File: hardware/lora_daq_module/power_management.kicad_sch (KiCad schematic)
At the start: 36 parts, among them J7 Conn_01x02, U6 MCP1700x-330xxTT, U7 TPS2116DRL, U8 TPS63002, U9 MCP73833

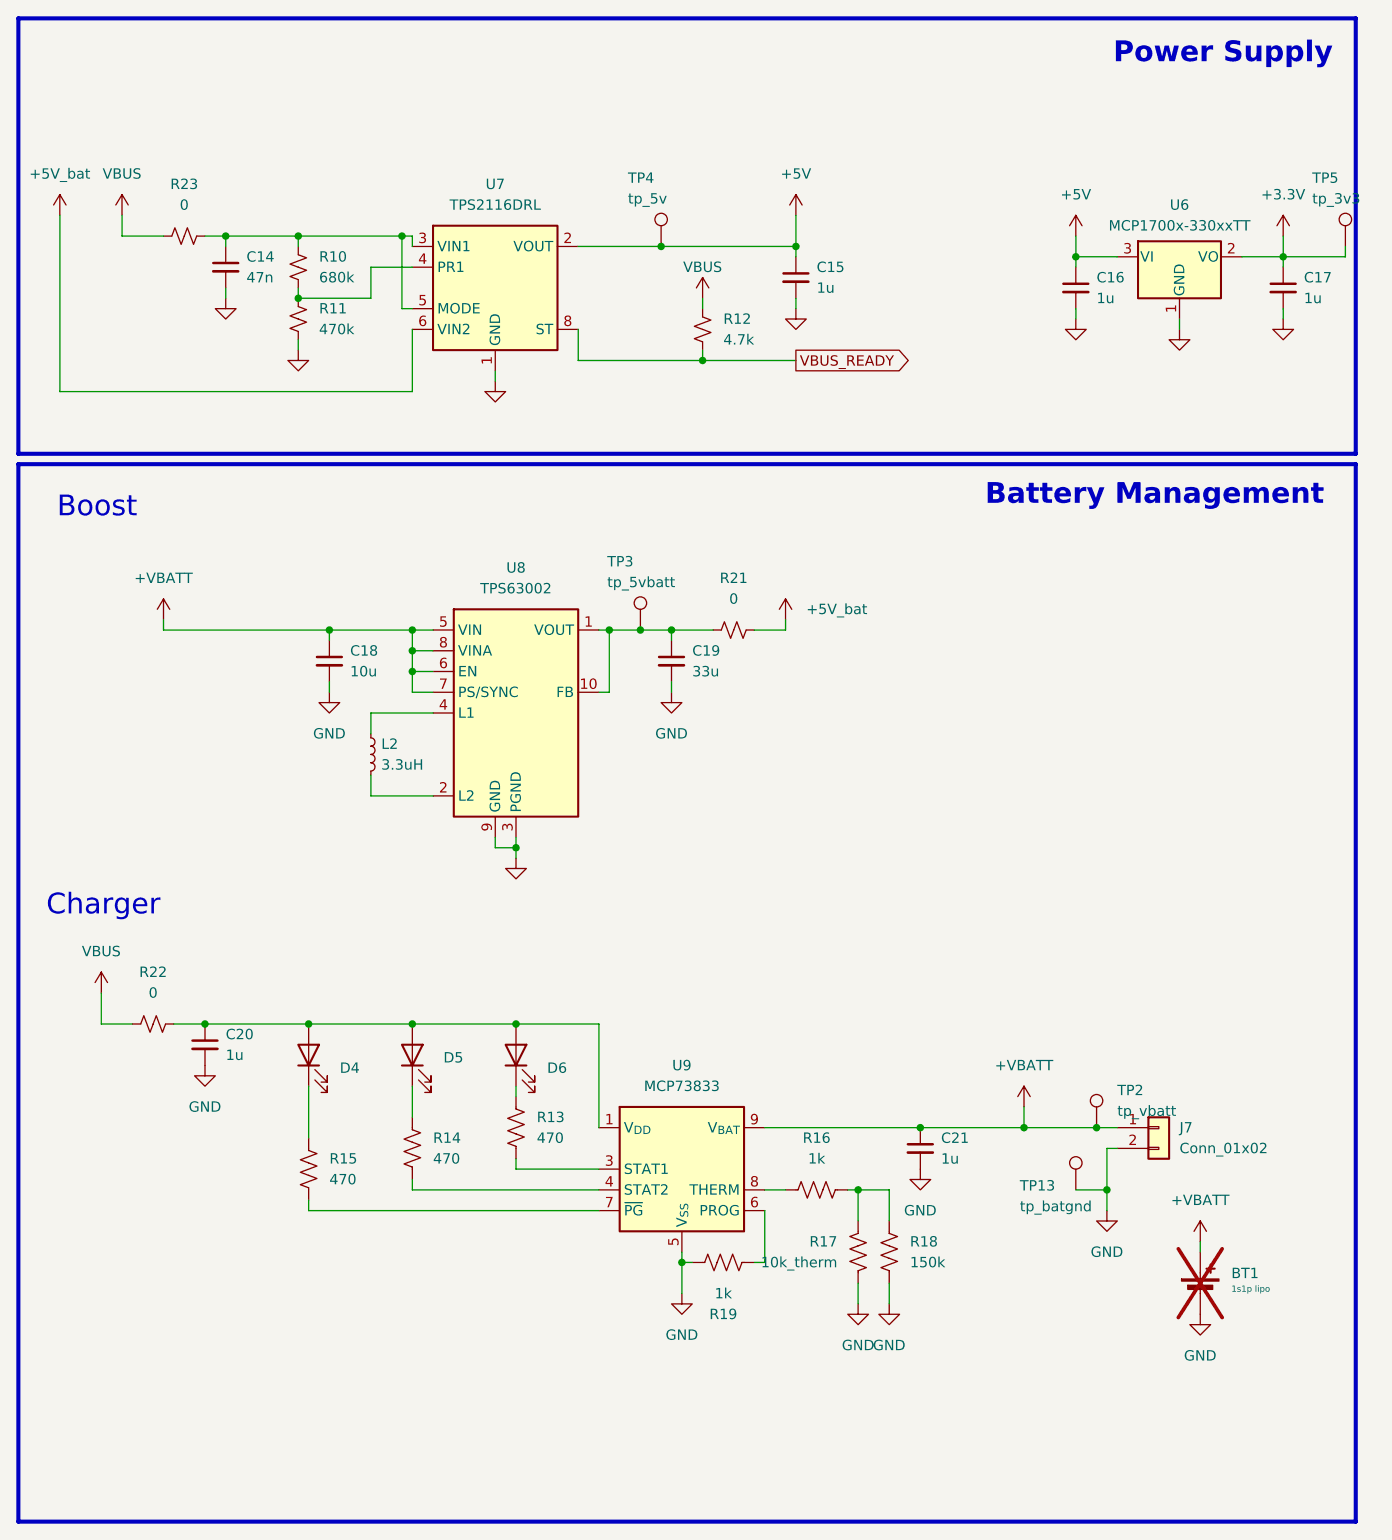
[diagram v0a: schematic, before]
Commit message: add 0Ω resistors for disabling power circuits, revise adc input buffer and filter based on design review feedback, revise microstrip trace, add hardware reset button, add i2c connector and jst receptacle for battery
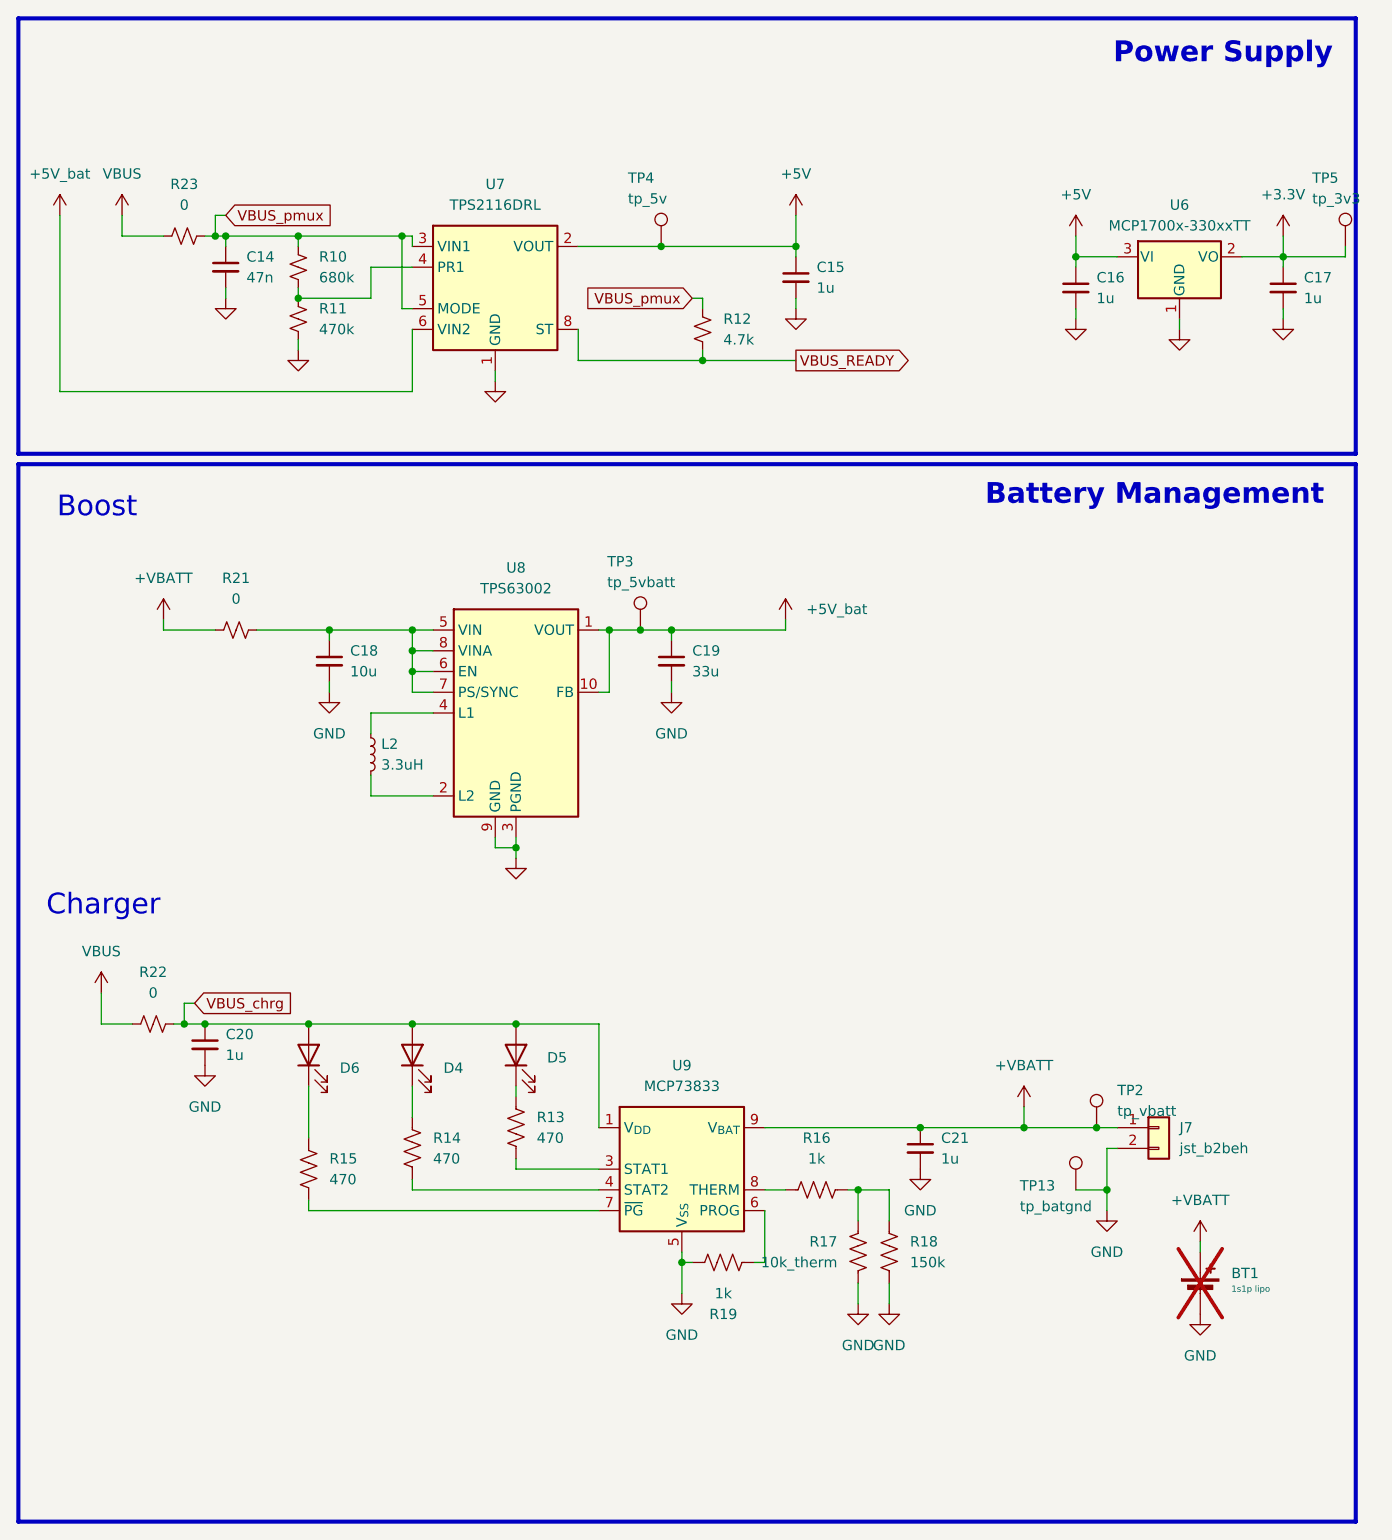
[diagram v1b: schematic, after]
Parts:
- BT1: Desc (none) -> 3.7 V Lithium-Ion Battery Rechargeable (Secondary) 1.2Ah; Dist (none) -> Digikey; Dist PN (none) -> 1528-1838-ND; Mfr (none) -> Adafruit Industries LLC; Mfr PN (none) -> 258
- J7: value Conn_01x02 -> jst_b2beh; footprint Connector_PinHeader_2.54mm:PinHeader_1x02_P2.54mm_Vertical -> Connector_JST:JST_EH_B2B-EH-A_1x02_P2.50mm_Vertical; Desc Connector Header Through Hole 2 position 0.100" (2.54mm) -> Connector Header Through Hole 2 position 0.098" (2.50mm); Dist PN 732-5315-ND -> 455-B2B-EH-A-ND; Mfr Würth Elektronik -> JST Sales America Inc.; Mfr PN 61300211121 -> B2B-EH-A
- R21, R22, R23: Desc (none) -> 0 Ohms Jumper Chip Resistor 1812 (4532 Metric) Automotive A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; Dist (none) -> Digikey; Dist PN (none) -> P122643CT-ND; Mfr (none) -> Panasonic Electronic Components; Mfr PN (none) -> ERJ-12Y0R00U
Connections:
- net +5V_bat: now also C19.1, TP3.1, U8.1 (VOUT), U8.10 (FB); no longer R21.2
- net +VBATT: now also R21.1; no longer C18.1, U8.5 (VIN), U8.6 (EN), U8.7 (PS/SYNC), U8.8 (VINA)
- net VBUS: no longer R12.1
- net at R13.1: now also D5.1 (K); no longer D6.1 (K)
- net VBUS_chrg: now reaches C20.1, D4.2 (A), D5.2 (A), D6.2 (A), R22.2, U9.1 (V_{DD}), U9.2 (V_{DD})
- net VBUS_pmux: now reaches C14.1, R10.1, R23.2, U7.3 (VIN1), U7.5 (MODE)
- net VBUS_pmux: now also R12.1
- net at R14.1: now also D4.1 (K); no longer D5.1 (K)
- net at R15.1: now also D6.1 (K); no longer D4.1 (K)
- new net: C18.1, R21.2, U8.5 (VIN), U8.6 (EN), U8.7 (PS/SYNC), U8.8 (VINA)
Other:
- moved on the sheet: D4, D5, D6, R21
